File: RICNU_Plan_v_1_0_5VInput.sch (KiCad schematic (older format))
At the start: 8 parts, among them J6 2x0.1, Q2 N-CH

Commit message: Added connections to monitor power, changed CANSTB MCU pin, moved LED pins around
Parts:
- D11: value TVS -> 5.0V TVS
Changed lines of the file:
@@
 P 6150 4050
 F 0 "D11" V 6300 3950 50  0000 C CNN
-F 1 "TVS" V 6000 3950 50  0000 C CNN
+F 1 "5.0V TVS" V 6000 3950 50  0000 C CNN
 F 2 "Diodes_SMD:D_SOD-523" H 6150 4050 50  0001 C CNN
 F 3 "" H 6150 4050 50  0001 C CNN
@@
 $EndComp
 $Comp
-L GND #PWR078
+L GND #PWR079
 U 1 1 59FB6623
 P 4250 4400
-F 0 "#PWR078" H 4250 4150 50  0001 C CNN
+F 0 "#PWR079" H 4250 4150 50  0001 C CNN
 F 1 "GND" H 4250 4250 50  0000 C CNN
 F 2 "" H 4250 4400 50  0001 C CNN
@@
 DF2B7AFS,L3M
 $Comp
-L +5V_EXT #PWR079
+L +5V_EXT #PWR080
 U 1 1 59FB6643
 P 6750 3700
-F 0 "#PWR079" H 6750 3550 50  0001 C CNN
+F 0 "#PWR080" H 6750 3550 50  0001 C CNN
 F 1 "+5V_EXT" H 6750 3840 50  0000 C CNN
 F 2 "" H 6750 3700 50  0001 C CNN
@@
 $EndComp
 $Comp
-L +5V_EXT_P #PWR080
+L +5V_EXT_P #PWR081
 U 1 1 59FB6649
 P 4250 3700
-F 0 "#PWR080" H 4250 3550 50  0001 C CNN
+F 0 "#PWR081" H 4250 3550 50  0001 C CNN
 F 1 "+5V_EXT_P" H 4250 3840 50  0000 C CNN
 F 2 "" H 4250 3700 50  0001 C CNN
@@
 GND_5V_INPUT
 $Comp
-L PWR_FLAG #FLG081
+L PWR_FLAG #FLG082
 U 1 1 59FD51B4
 P 6750 4400
-F 0 "#FLG081" H 6750 4475 50  0001 C CNN
+F 0 "#FLG082" H 6750 4475 50  0001 C CNN
 F 1 "PWR_FLAG" H 6750 4550 50  0000 C CNN
 F 2 "" H 6750 4400 50  0001 C CNN

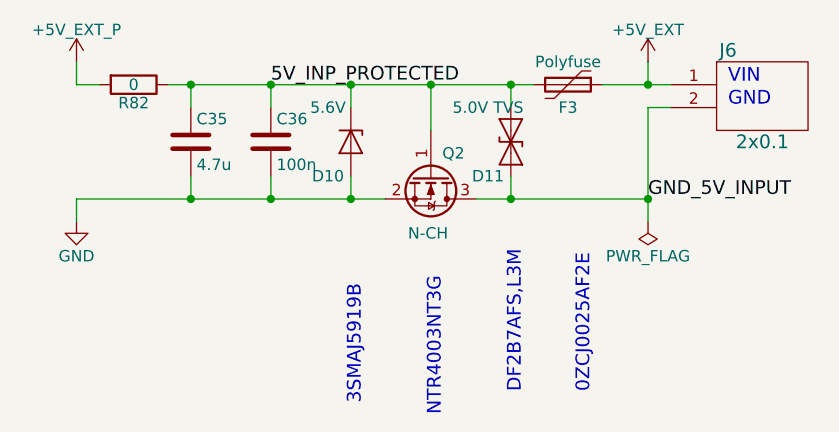
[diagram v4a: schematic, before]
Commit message: Various small changes like comment removal
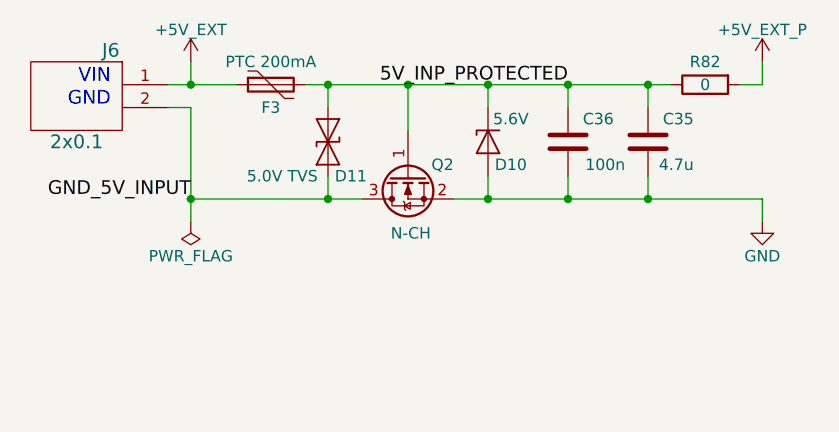
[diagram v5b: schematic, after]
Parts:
- F3: value Polyfuse -> PTC 200mA
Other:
- note removed: "0ZCJ0025AF2E"
- note removed: "3SMAJ5919B"
- note removed: "DF2B7AFS,L3M"
- note removed: "NTR4003NT3G"
- moved on the sheet: C35, C36, D10, D11, F3, J6, Q2, R82
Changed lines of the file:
@@
 L D_TVS D11
 U 1 1 59FB6607
-P 6150 4050
-F 0 "D11" V 6300 3950 50  0000 C CNN
-F 1 "5.0V TVS" V 6000 3950 50  0000 C CNN
-F 2 "Diodes_SMD:D_SOD-523" H 6150 4050 50  0001 C CNN
-F 3 "" H 6150 4050 50  0001 C CNN
-	1    6150 4050
-	0    1    1    0
+P 5350 4050
+F 0 "D11" V 5500 3950 50  0000 C CNN
+F 1 "5.0V TVS" V 5500 4250 50  0000 C CNN
+F 2 "Diodes_SMD:D_SOD-523" H 5350 4050 50  0001 C CNN
+F 3 "" H 5350 4050 50  0001 C CNN
+	1    5350 4050
+	0    -1   1    0
 $EndComp
 $Comp
 L D_Zener D10
 U 1 1 59FB660E
-P 5450 4050
-F 0 "D10" V 5600 3950 50  0000 C CNN
-F 1 "5.6V" V 5300 3950 50  0000 C CNN
-F 2 "Diodes_SMD:D_SMA_Handsoldering" H 5450 4050 50  0001 C CNN
-F 3 "" H 5450 4050 50  0001 C CNN
-	1    5450 4050
-	0    1    1    0
+P 6050 4050
+F 0 "D10" V 6150 3950 50  0000 C CNN
+F 1 "5.6V" V 5950 3950 50  0000 C CNN
+F 2 "Diodes_SMD:D_SMA_Handsoldering" H 6050 4050 50  0001 C CNN
+F 3 "" H 6050 4050 50  0001 C CNN
+	1    6050 4050
+	0    -1   1    0
 $EndComp
 $Comp
 L Polyfuse F3
 U 1 1 59FB6615
-P 6400 3800
-F 0 "F3" V 6500 3800 50  0000 C CNN
-F 1 "Polyfuse" V 6300 3800 50  0000 C CNN
-F 2 "Resistors_SMD:R_0603_HandSoldering" H 6450 3600 50  0001 L CNN
-F 3 "" H 6400 3800 50  0001 C CNN
-	1    6400 3800
-	0    1    1    0
+P 5100 3800
+F 0 "F3" V 5200 3800 50  0000 C CNN
+F 1 "PTC 200mA" V 5000 3800 50  0000 C CNN
+F 2 "Resistors_SMD:R_0603_HandSoldering" H 5150 3600 50  0001 L CNN
+F 3 "" H 5100 3800 50  0001 C CNN
+	1    5100 3800
+	0    -1   1    0
 $EndComp
 $Comp
 L C C36
 U 1 1 59FB661C
-P 5100 4050
-F 0 "C36" H 5125 4150 50  0000 L CNN
-F 1 "100n" H 5125 3950 50  0000 L CNN
-F 2 "Capacitors_SMD:C_0402_NoSilk" H 5138 3900 50  0001 C CNN
-F 3 "" H 5100 4050 50  0001 C CNN
-	1    5100 4050
-	1    0    0    -1
+P 6400 4050
+F 0 "C36" H 6200 4150 50  0000 L CNN
+F 1 "100n" H 6150 3950 50  0000 L CNN
+F 2 "Capacitors_SMD:C_0402_NoSilk" H 6438 3900 50  0001 C CNN
+F 3 "" H 6400 4050 50  0001 C CNN
+	1    6400 4050
+	-1   0    0    -1
 $EndComp
 $Comp
 L GND #PWR084
 U 1 1 59FB6623
-P 4250 4400
-F 0 "#PWR084" H 4250 4150 50  0001 C CNN
-F 1 "GND" H 4250 4250 50  0000 C CNN
-F 2 "" H 4250 4400 50  0001 C CNN
-F 3 "" H 4250 4400 50  0001 C CNN
-	1    4250 4400
-	1    0    0    -1
+P 7250 4400
+F 0 "#PWR084" H 7250 4150 50  0001 C CNN
+F 1 "GND" H 7250 4250 50  0000 C CNN
+F 2 "" H 7250 4400 50  0001 C CNN
+F 3 "" H 7250 4400 50  0001 C CNN
+	1    7250 4400
+	-1   0    0    -1
 $EndComp
 $Comp
 L Q_NMOS_GSD Q2
 U 1 1 59FB6630
-P 5800 4200
-F 0 "Q2" V 5700 4250 50  0000 L CNN
-F 1 "N-CH" V 6050 4100 50  0000 L CNN
-F 2 "TO_SOT_Packages_SMD:SOT-23" H 6000 4300 50  0001 C CNN
-F 3 "" H 5800 4200 50  0001 C CNN
-	1    5800 4200
-	0    1    1    0
+P 5700 4200
+F 0 "Q2" V 5650 4000 50  0000 L CNN
+F 1 "N-CH" V 5950 4100 50  0000 L CNN
+F 2 "TO_SOT_Packages_SMD:SOT-23" H 5900 4300 50  0001 C CNN
+F 3 "" H 5700 4200 50  0001 C CNN
+	1    5700 4200
+	0    -1   1    0
 $EndComp
 $Comp
 L C C35
 U 1 1 59FB6638
-P 4750 4050
-F 0 "C35" H 4775 4150 50  0000 L CNN
-F 1 "4.7u" H 4775 3950 50  0000 L CNN
-F 2 "Capacitors_SMD:C_0805" H 4788 3900 50  0001 C CNN
-F 3 "" H 4750 4050 50  0001 C CNN
-	1    4750 4050
-	1    0    0    -1
+P 6750 4050
+F 0 "C35" H 6550 4150 50  0000 L CNN
+F 1 "4.7u" H 6550 3950 50  0000 L CNN
+F 2 "Capacitors_SMD:C_0805" H 6788 3900 50  0001 C CNN
+F 3 "" H 6750 4050 50  0001 C CNN
+	1    6750 4050
+	-1   0    0    -1
 $EndComp
-Text Notes 5850 5250 1    60   ~ 0
-NTR4003NT3G
-Text Notes 5500 5200 1    60   ~ 0
-3SMAJ5919B
-Text Notes 6500 5150 1    60   ~ 0
-0ZCJ0025AF2E
-Text Notes 6200 5150 1    60   ~ 0
-DF2B7AFS,L3M
 $Comp
 L +5V_EXT #PWR085
 U 1 1 59FB6643
-P 6750 3700
-F 0 "#PWR085" H 6750 3550 50  0001 C CNN
-F 1 "+5V_EXT" H 6750 3840 50  0000 C CNN
-F 2 "" H 6750 3700 50  0001 C CNN
-F 3 "" H 6750 3700 50  0001 C CNN
-	1    6750 3700
-	1    0    0    -1
+P 4750 3700
+F 0 "#PWR085" H 4750 3550 50  0001 C CNN
+F 1 "+5V_EXT" H 4750 3840 50  0000 C CNN
+F 2 "" H 4750 3700 50  0001 C CNN
+F 3 "" H 4750 3700 50  0001 C CNN
+	1    4750 3700
+	-1   0    0    -1
 $EndComp
 $Comp
 L +5V_EXT_P #PWR086
 U 1 1 59FB6649
-P 4250 3700
-F 0 "#PWR086" H 4250 3550 50  0001 C CNN
-F 1 "+5V_EXT_P" H 4250 3840 50  0000 C CNN
-F 2 "" H 4250 3700 50  0001 C CNN
-F 3 "" H 4250 3700 50  0001 C CNN
-	1    4250 3700
-	1    0    0    -1
+P 7250 3700
+F 0 "#PWR086" H 7250 3550 50  0001 C CNN
+F 1 "+5V_EXT_P" H 7250 3840 50  0000 C CNN
+F 2 "" H 7250 3700 50  0001 C CNN
+F 3 "" H 7250 3700 50  0001 C CNN
+	1    7250 3700
+	-1   0    0    -1
 $EndComp
-Connection ~ 4750 3800
-Connection ~ 4750 4300
+Connection ~ 6750 3800
+Connection ~ 6750 4300
 $Comp
 L R R82
 U 1 1 59FB6664
-P 4500 3800
-F 0 "R82" V 4580 3800 50  0000 C CNN
-F 1 "0" V 4500 3800 50  0000 C CNN
-F 2 "Resistors_SMD:R_0402_NoSilk" V 4430 3800 50  0001 C CNN
-F 3 "" H 4500 3800 50  0001 C CNN
-	1    4500 3800
-	0    1    1    0
+P 7000 3800
+F 0 "R82" V 6900 3800 50  0000 C CNN
+F 1 "0" V 7000 3800 50  0000 C CNN
+F 2 "Resistors_SMD:R_0402_NoSilk" V 6930 3800 50  0001 C CNN
+F 3 "" H 7000 3800 50  0001 C CNN
+	1    7000 3800
+	0    -1   1    0
 $EndComp
 $Comp
 L 2x0.1 J6
 U 1 1 59FC84C7
-P 7250 3850
-F 0 "J6" H 7100 4050 60  0000 C CNN
-F 1 "2x0.1" H 7250 3650 60  0000 C CNN
-F 2 "Pin_Headers:Pin_Header_Straight_1x02_Pitch2.54mm" H 7250 3850 60  0001 C CNN
-F 3 "" H 7250 3850 60  0001 C CNN
-	1    7250 3850
-	1    0    0    -1
+P 4250 3850
+F 0 "J6" H 4100 4050 60  0000 C CNN
+F 1 "2x0.1" H 4250 3650 60  0000 C CNN
+F 2 "Pin_Headers:Pin_Header_Straight_1x02_Pitch2.54mm" H 4250 3850 60  0001 C CNN
+F 3 "" H 4250 3850 60  0001 C CNN
+	1    4250 3850
+	-1   0    0    -1
 $EndComp
 Wire Wire Line
-	4650 3800 6250 3800
+	6850 3800 5250 3800
 Wire Wire Line
-	6550 3800 6850 3800
+	4950 3800 4650 3800
 Wire Wire Line
-	4250 4300 5600 4300
+	7250 4300 5900 4300
 Wire Wire Line
-	6000 4300 6750 4300
+	5500 4300 4750 4300
 Wire Wire Line
-	6750 3900 6750 4400
+	4750 3900 4750 4400
 Wire Wire Line
-	6750 3900 6850 3900
+	4750 3900 4650 3900
 Wire Wire Line
-	6150 4200 6150 4300
-Connection ~ 6150 4300
+	5350 4200 5350 4300
+Connection ~ 5350 4300
 Wire Wire Line
-	6150 3900 6150 3800
-Connection ~ 6150 3800
+	5350 3900 5350 3800
+Connection ~ 5350 3800
 Wire Wire Line
-	5800 4000 5800 3800
-Connection ~ 5800 3800
+	5700 4000 5700 3800
+Connection ~ 5700 3800
 Wire Wire Line
-	5450 3900 5450 3800
-Connection ~ 5450 3800
+	6050 3900 6050 3800
+Connection ~ 6050 3800
 Wire Wire Line
-	5100 3900 5100 3800
-Connection ~ 5100 3800
+	6400 3900 6400 3800
+Connection ~ 6400 3800
 Wire Wire Line
-	6750 3700 6750 3800
-Connection ~ 6750 3800
-Text Notes 7100 3800 0    60   ~ 0
+	4750 3700 4750 3800
+Connection ~ 4750 3800
+Text Notes 4400 3800 2    60   ~ 0
 VIN
-Text Notes 7100 3900 0    60   ~ 0
+Text Notes 4400 3900 2    60   ~ 0
 GND
 Wire Wire Line
-	5100 4200 5100 4300
-Connection ~ 5100 4300
+	6400 4200 6400 4300
+Connection ~ 6400 4300
 Wire Wire Line
-	5450 4200 5450 4300
-Connection ~ 5450 4300
+	6050 4200 6050 4300
+Connection ~ 6050 4300
 Wire Wire Line
-	4350 3800 4250 3800
+	7150 3800 7250 3800
 Wire Wire Line
-	4250 3800 4250 3700
+	7250 3800 7250 3700
 Wire Wire Line
-	4750 3900 4750 3800
+	6750 3900 6750 3800
 Wire Wire Line
-	4250 4300 4250 4400
+	7250 4300 7250 4400
 Wire Wire Line
-	4750 4300 4750 4200
-Text Label 6750 4300 0    60   ~ 0
+	6750 4300 6750 4200
+Text Label 4750 4300 2    60   ~ 0
 GND_5V_INPUT
 $Comp
 L PWR_FLAG #FLG087
 U 1 1 59FD51B4
-P 6750 4400
-F 0 "#FLG087" H 6750 4475 50  0001 C CNN
-F 1 "PWR_FLAG" H 6750 4550 50  0000 C CNN
-F 2 "" H 6750 4400 50  0001 C CNN
-F 3 "" H 6750 4400 50  0001 C CNN
-	1    6750 4400
-	-1   0    0    1
+P 4750 4400
+F 0 "#FLG087" H 4750 4475 50  0001 C CNN
+F 1 "PWR_FLAG" H 4750 4550 50  0000 C CNN
+F 2 "" H 4750 4400 50  0001 C CNN
+F 3 "" H 4750 4400 50  0001 C CNN
+	1    4750 4400
+	1    0    0    1
 $EndComp
-Connection ~ 6750 4300
-Text Label 5100 3800 0    60   ~ 0
+Connection ~ 4750 4300
+Text Label 6400 3800 2    60   ~ 0
 5V_INP_PROTECTED
 $EndSCHEMATC
